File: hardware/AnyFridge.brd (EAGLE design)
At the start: 75.9 x 69.8 mm, 14 parts

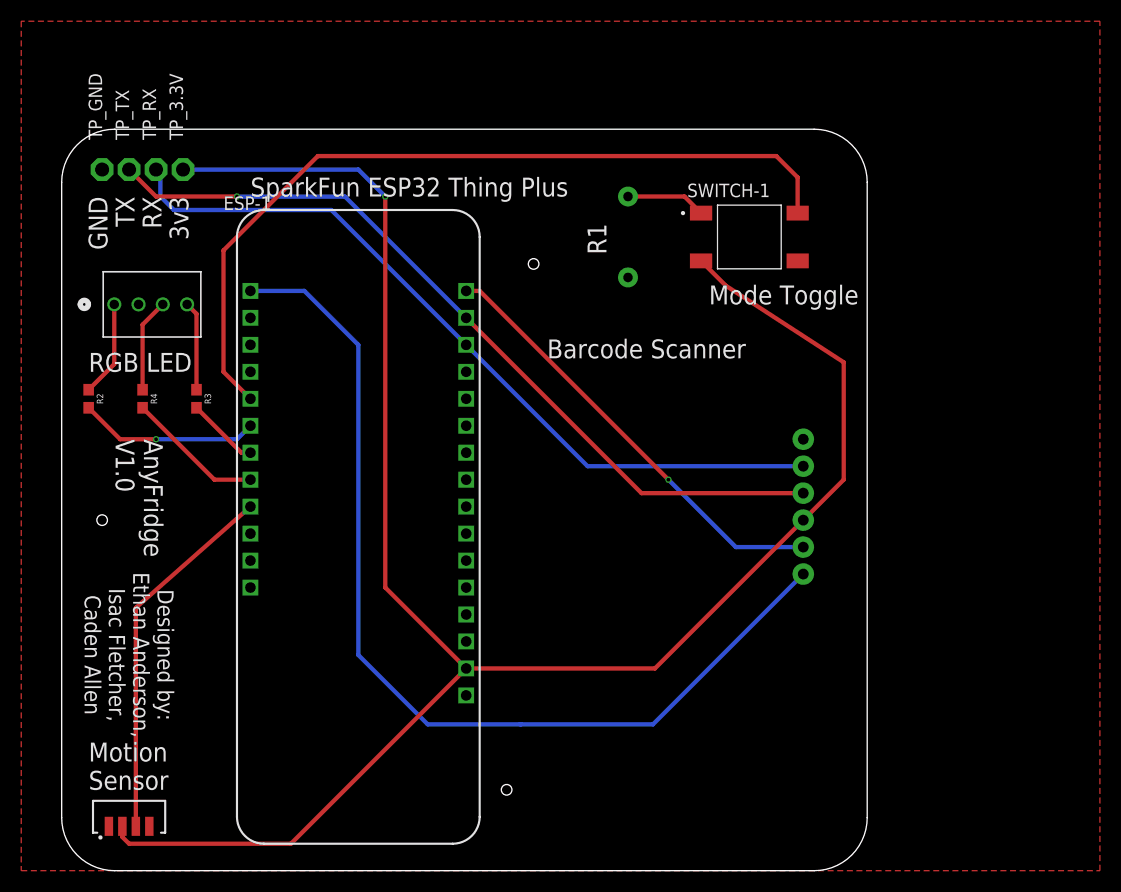
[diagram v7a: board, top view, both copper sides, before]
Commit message: move resistors to top layer
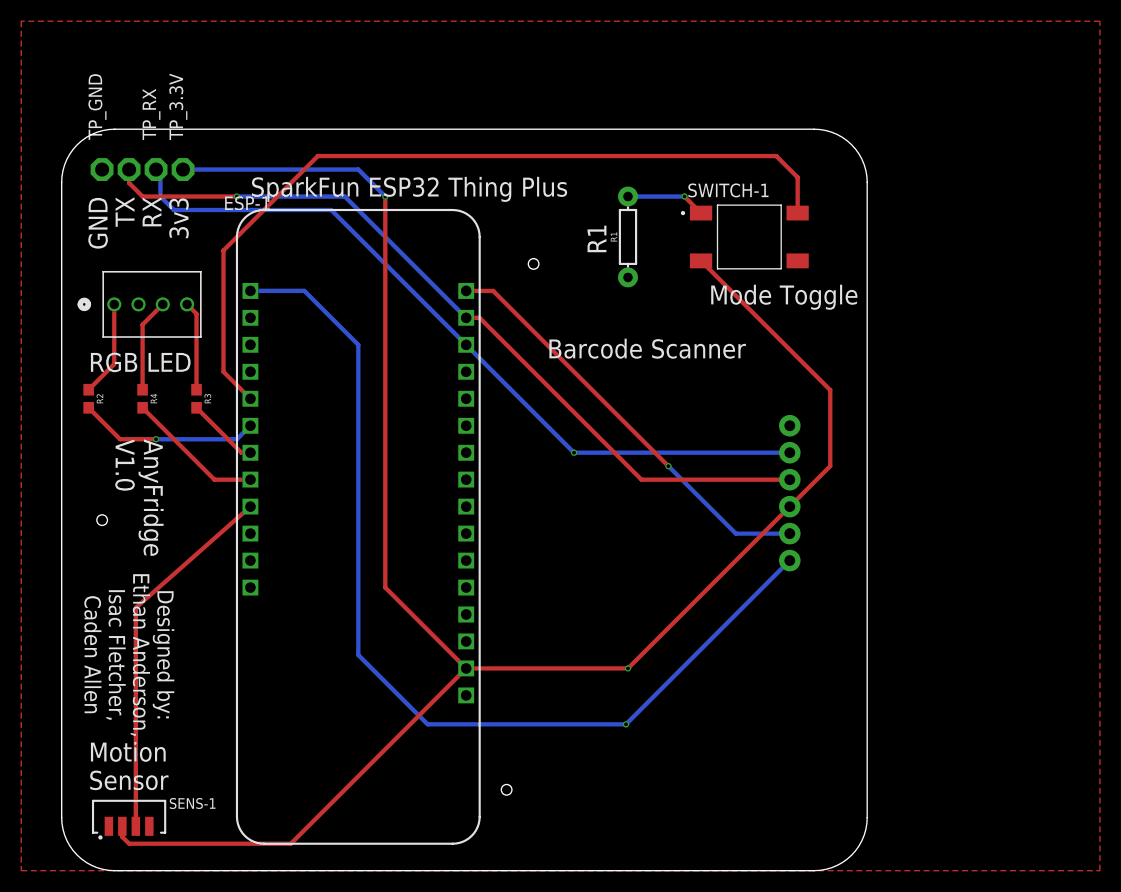
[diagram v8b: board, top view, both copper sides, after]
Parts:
- moved SCAN-1 1.80 mm to (47.0, 48.3)
- flipped R1 to the top
- flipped TP_TX to the top
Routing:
- net 3.3V: track 178.7 -> 174.8 mm, vias 1 -> 2
- net TRIG: track 41.7 -> 39.9 mm
- net RX1: track 73.8 -> 72.0 mm, vias 0 -> 1
- net TX1: track 76.1 -> 75.1 mm
- net STAT: track 92.0 -> 91.2 mm, vias 0 -> 1
- net N$1: vias 0 -> 1
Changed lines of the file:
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@@
 <attribute name="VALUE" x="7.7978" y="57.785" size="1.27" layer="27" ratio="6" rot="SR0"/>
 </element>
-<element name="R1" library="SparkFun-Resistors" library_urn="urn:adsk.eagle:library:532" package="AXIAL-0.3" package3d_urn="urn:adsk.eagle:package:39658/2" value="10k" x="55.88" y="59.69" smashed="yes" rot="MR90">
-<attribute name="NAME" x="56.896" y="59.69" size="0.6096" layer="26" font="vector" ratio="20" rot="MR90" align="bottom-center"/>
-<attribute name="PROD_ID" value="RES-12183" x="-97.79" y="95.25" size="1.778" layer="28" rot="MR90" display="off"/>
-<attribute name="VALUE" x="54.864" y="59.69" size="0.6096" layer="28" font="vector" ratio="20" rot="MR90" align="top-center"/>
+<element name="R1" library="SparkFun-Resistors" library_urn="urn:adsk.eagle:library:532" package="AXIAL-0.3" package3d_urn="urn:adsk.eagle:package:39658/2" value="10k" x="55.88" y="59.69" smashed="yes" rot="R90">
+<attribute name="NAME" x="54.864" y="59.69" size="0.6096" layer="25" font="vector" ratio="20" rot="R90" align="bottom-center"/>
+<attribute name="PROD_ID" value="RES-12183" x="209.55" y="95.25" size="1.778" layer="27" rot="R90" display="off"/>
+<attribute name="VALUE" x="56.896" y="59.69" size="0.6096" layer="27" font="vector" ratio="20" rot="R90" align="top-center"/>
 </element>
-<element name="SCAN-1" library="SEN-18088" package="SEN-18088" value="SEN-18088" x="48.26" y="46.99" smashed="yes" rot="MR270">
-<attribute name="NAME" x="46.99" y="44.45" size="1.27" layer="26" rot="MR270"/>
-<attribute name="VALUE" x="45.72" y="11.43" size="1.27" layer="28" rot="MR270"/>
+<element name="SCAN-1" library="SEN-18088" package="SEN-18088" value="SEN-18088" x="46.99" y="48.26" smashed="yes" rot="MR270">
+<attribute name="NAME" x="45.72" y="45.72" size="1.27" layer="26" rot="MR270"/>
+<attribute name="VALUE" x="44.45" y="12.7" size="1.27" layer="28" rot="MR270"/>
 </element>
 <element name="SENS-1" library="MISC-PARTS" package="TSSP77038TT" package3d_urn="urn:adsk.eagle:package:47059864/1" value="TSSP77038TT" x="8.89" y="5.08" smashed="yes">
@@
 <attribute name="MF" value="Vishay" x="35.56" y="-148.59" size="1.778" layer="27" display="off"/>
 <attribute name="MP" value="TSSP77038TT" x="35.56" y="-148.59" size="1.778" layer="27" display="off"/>
+<attribute name="NAME" x="12.64" y="5.83" size="1" layer="51" ratio="21" rot="SR0"/>
 <attribute name="NAME" x="12.64" y="5.83" size="1" layer="25" ratio="20" rot="SR0"/>
-<attribute name="NAME" x="12.64" y="5.83" size="1" layer="51" ratio="21" rot="SR0"/>
 <attribute name="PACKAGE" value="None" x="35.56" y="-148.59" size="1.778" layer="27" display="off"/>
 <attribute name="PRICE" value="None" x="35.56" y="-148.59" size="1.778" layer="27" display="off"/>
@@
 <attribute name="VALUE" x="2.54" y="66.04" size="0.0254" layer="28" rot="MR270"/>
 </element>
-<element name="TP_TX" library="testpad" library_urn="urn:adsk.eagle:library:385" package="P1-13" package3d_urn="urn:adsk.eagle:package:27946/1" value="TPPAD1-13" x="8.89" y="66.04" smashed="yes" rot="MR90">
-<attribute name="NAME" x="8.89" y="68.834" size="1.27" layer="25" ratio="10" rot="R90"/>
-<attribute name="POPULARITY" value="12" x="8.89" y="66.04" size="1.778" layer="28" rot="MR90" display="off"/>
-<attribute name="TP_SIGNAL_NAME" value="" x="8.89" y="66.04" size="1.778" layer="28" rot="MR90" display="off"/>
-<attribute name="VALUE" x="10.16" y="63.5" size="0.0254" layer="27" rot="R270"/>
+<element name="TP_TX" library="testpad" library_urn="urn:adsk.eagle:library:385" package="P1-13" package3d_urn="urn:adsk.eagle:package:27946/1" value="TPPAD1-13" x="8.89" y="66.04" smashed="yes" rot="R90">
+<attribute name="NAME" x="8.89" y="68.834" size="1.27" layer="26" ratio="10" rot="MR90"/>
+<attribute name="POPULARITY" value="12" x="8.89" y="66.04" size="1.778" layer="27" rot="R90" display="off"/>
+<attribute name="TP_SIGNAL_NAME" value="" x="8.89" y="66.04" size="1.778" layer="27" rot="R90" display="off"/>
+<attribute name="VALUE" x="7.62" y="63.5" size="0.0254" layer="28" rot="MR270"/>
 </element>
 <element name="TP_RX" library="testpad" library_urn="urn:adsk.eagle:library:385" package="P1-13" package3d_urn="urn:adsk.eagle:package:27946/1" value="TPPAD1-13" x="11.43" y="66.04" smashed="yes" rot="R90">
@@
 <wire x1="33.02" y1="26.67" x2="33.02" y2="63.5" width="0.4064" layer="1"/>
 <via x="33.02" y="63.5" extent="1-16" drill="0.35"/>
-<wire x1="40.64" y1="19.05" x2="58.42" y2="19.05" width="0.4064" layer="1"/>
-<wire x1="58.42" y1="19.05" x2="72.39" y2="33.02" width="0.4064" layer="1"/>
+<wire x1="40.64" y1="19.05" x2="55.88" y2="19.05" width="0.4064" layer="1"/>
+<wire x1="55.88" y1="19.05" x2="71.12" y2="34.29" width="0.4064" layer="1"/>
 <wire x1="33.02" y1="63.5" x2="30.48" y2="66.04" width="0.4064" layer="16"/>
-<wire x1="72.39" y1="33.02" x2="76.2" y2="36.83" width="0.4064" layer="1"/>
-<wire x1="76.2" y1="36.83" x2="76.2" y2="47.885065625" width="0.4064" layer="1"/>
-<wire x1="76.2" y1="47.885065625" x2="65.11395" y2="55.08605" width="0.4064" layer="1"/>
-<wire x1="65.11395" y1="55.08605" x2="62.76" y2="57.44" width="0.4064" layer="1"/>
+<wire x1="71.12" y1="34.29" x2="74.93" y2="38.1" width="0.4064" layer="1"/>
+<via x="55.88" y="19.05" extent="1-16" drill="0.35"/>
+<wire x1="74.93" y1="38.1" x2="74.93" y2="45.27" width="0.4064" layer="1"/>
+<wire x1="74.93" y1="45.27" x2="62.76" y2="57.44" width="0.4064" layer="1"/>
 </signal>
 <signal name="TRIG">
 <contactref element="SCAN-1" pad="TRIG"/>
 <contactref element="ESP-1" pad="21"/>
-<wire x1="59.69" y1="36.83" x2="41.91" y2="54.61" width="0.4064" layer="1"/>
-<wire x1="40.64" y1="54.61" x2="41.91" y2="54.61" width="0.4064" layer="1"/>
-<via x="59.69" y="36.83" extent="1-16" drill="0.35"/>
-<wire x1="66.04" y1="30.48" x2="59.69" y2="36.83" width="0.4064" layer="16"/>
-<wire x1="66.04" y1="30.48" x2="72.39" y2="30.48" width="0.4064" layer="16"/>
+<wire x1="59.69" y1="38.1" x2="43.18" y2="54.61" width="0.4064" layer="1"/>
+<wire x1="40.64" y1="54.61" x2="43.18" y2="54.61" width="0.4064" layer="1"/>
+<via x="59.69" y="38.1" extent="1-16" drill="0.35"/>
+<wire x1="59.69" y1="38.1" x2="66.04" y2="31.75" width="0.4064" layer="16"/>
+<wire x1="66.04" y1="31.75" x2="71.12" y2="31.75" width="0.4064" layer="16"/>
 </signal>
 <signal name="STAT">
@@
 <wire x1="30.48" y1="49.53" x2="25.4" y2="54.61" width="0.4064" layer="16"/>
 <wire x1="20.32" y1="54.61" x2="25.4" y2="54.61" width="0.4064" layer="16"/>
-<wire x1="37.015496875" y1="13.784503125" x2="45.72" y2="13.784503125" width="0.4064" layer="16"/>
-<wire x1="45.72" y1="13.784503125" x2="45.807071875" y2="13.784503125" width="0.4064" layer="16"/>
 <wire x1="37.015496875" y1="13.784503125" x2="30.48" y2="20.32" width="0.4064" layer="16"/>
 <wire x1="30.48" y1="20.32" x2="30.48" y2="49.53" width="0.4064" layer="16"/>
-<wire x1="45.807071875" y1="13.784503125" x2="58.234503125" y2="13.784503125" width="0.4064" layer="16"/>
-<wire x1="58.234503125" y1="13.784503125" x2="72.39" y2="27.94" width="0.4064" layer="16"/>
+<wire x1="37.015496875" y1="13.784503125" x2="55.694503125" y2="13.784503125" width="0.4064" layer="16"/>
+<wire x1="55.694503125" y1="13.784503125" x2="71.12" y2="29.21" width="0.4064" layer="16"/>
+<via x="55.694503125" y="13.784503125" extent="1-16" drill="0.35"/>
 </signal>
 <signal name="BLUE">
@@
 <contactref element="SWITCH-1" pad="1"/>
 <contactref element="R1" pad="P$2"/>
-<wire x1="55.88" y1="63.5" x2="61.2" y2="63.5" width="0.4064" layer="1"/>
+<wire x1="55.88" y1="63.5" x2="61.2" y2="63.5" width="0.4064" layer="16"/>
 <wire x1="61.2" y1="63.5" x2="62.76" y2="61.94" width="0.4064" layer="1"/>
+<via x="61.2" y="63.5" extent="1-16" drill="0.35"/>
 </signal>
 <signal name="TX1">
@@
 <contactref element="SCAN-1" pad="RX"/>
 <contactref element="TP_TX" pad="TP"/>
-<wire x1="11.43" y1="63.5" x2="19.05" y2="63.5" width="0.4064" layer="1"/>
-<wire x1="11.43" y1="63.5" x2="8.89" y2="66.04" width="0.4064" layer="1"/>
+<wire x1="19.05" y1="63.5" x2="10.16" y2="63.5" width="0.4064" layer="1"/>
 <via x="19.05" y="63.5" extent="1-16" drill="0.35"/>
 <wire x1="19.05" y1="63.5" x2="29.21" y2="63.5" width="0.4064" layer="16"/>
 <wire x1="29.21" y1="63.5" x2="40.64" y2="52.07" width="0.4064" layer="16"/>
-<wire x1="40.64" y1="52.07" x2="57.15" y2="35.56" width="0.4064" layer="1"/>
-<wire x1="57.15" y1="35.56" x2="72.39" y2="35.56" width="0.4064" layer="1"/>
+<wire x1="40.64" y1="52.07" x2="41.91" y2="52.07" width="0.4064" layer="1"/>
+<wire x1="57.15" y1="36.83" x2="41.91" y2="52.07" width="0.4064" layer="1"/>
+<wire x1="10.16" y1="63.5" x2="8.89" y2="64.77" width="0.4064" layer="1"/>
+<wire x1="8.89" y1="64.77" x2="8.89" y2="66.04" width="0.4064" layer="1"/>
+<wire x1="57.15" y1="36.83" x2="71.12" y2="36.83" width="0.4064" layer="1"/>
 </signal>
 <signal name="RX1">
@@
 <wire x1="40.64" y1="49.53" x2="27.94" y2="62.23" width="0.4064" layer="16"/>
 <wire x1="27.94" y1="62.23" x2="13.11185" y2="62.23" width="0.4064" layer="16"/>
-<wire x1="40.64" y1="49.53" x2="52.07" y2="38.1" width="0.4064" layer="16"/>
-<wire x1="52.07" y1="38.1" x2="72.39" y2="38.1" width="0.4064" layer="16"/>
+<wire x1="40.64" y1="49.53" x2="50.8" y2="39.37" width="0.4064" layer="16"/>
+<wire x1="50.8" y1="39.37" x2="71.12" y2="39.37" width="0.4064" layer="16"/>
+<via x="50.8" y="39.37" extent="1-16" drill="0.35"/>
 </signal>
 <signal name="SWI-OUT">
